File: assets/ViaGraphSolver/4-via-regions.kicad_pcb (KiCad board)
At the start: 2 copper layers, 0 parts

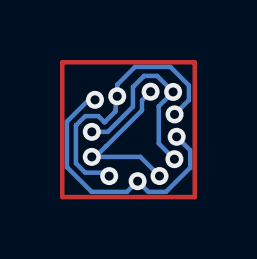
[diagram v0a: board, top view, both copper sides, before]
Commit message: 4 via region topology optimization
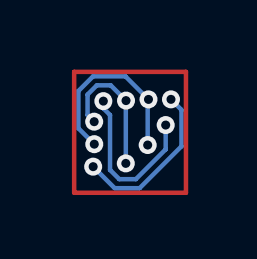
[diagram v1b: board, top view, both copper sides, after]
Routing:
- net Net6: track 9.21 -> 0.00 mm, vias 3 -> 0
- net Net8: track 9.05 -> 0.00 mm, vias 3 -> 0
- net Net7: track 6.74 -> 0.00 mm, vias 3 -> 0
- net net5: track 0.00 -> 6.40 mm, vias 0 -> 3
- net net1: track 0.00 -> 5.59 mm, vias 0 -> 2
- net Net5: track 5.58 -> 0.00 mm, vias 3 -> 0
- net net3: track 0.00 -> 5.53 mm, vias 0 -> 2
- net net4: track 0.00 -> 4.71 mm, vias 0 -> 3
